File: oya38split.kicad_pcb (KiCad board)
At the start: 2 copper layers, 89 parts, among them M12 MX-NoLED, U1 ProMicro

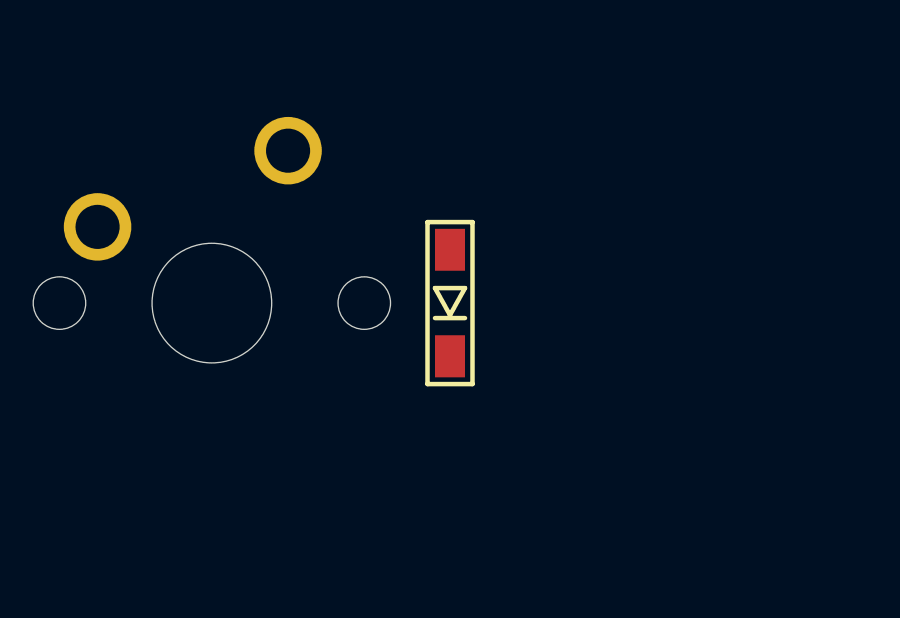
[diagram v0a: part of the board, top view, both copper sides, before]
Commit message: fixed diode alignment
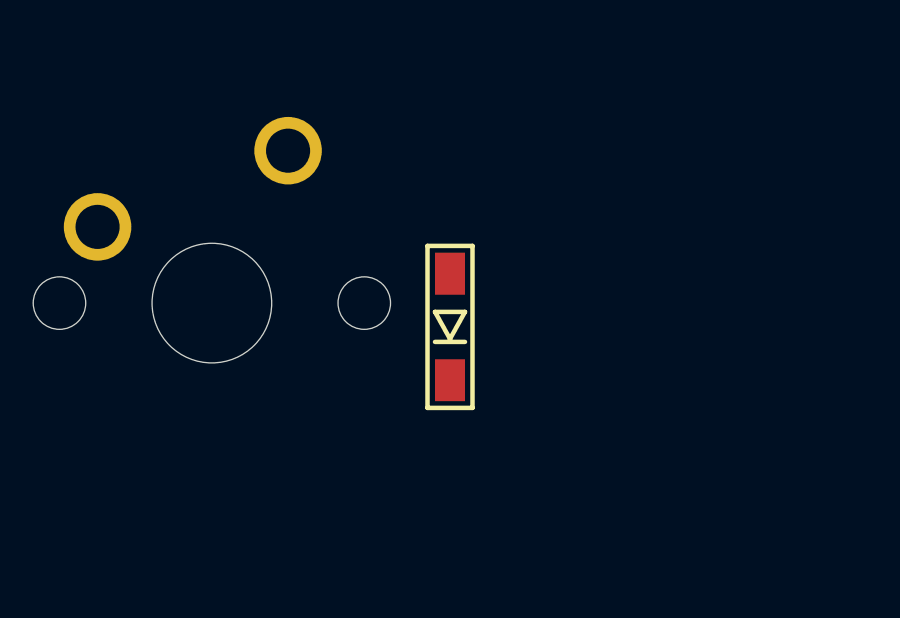
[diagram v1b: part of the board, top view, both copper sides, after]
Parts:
- moved D31 0.79 mm to (65.1, 115.1)
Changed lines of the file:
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@@
   )
   (module kbd:D3_SMD_v2 (layer F.Cu)
-    (at 65.0875 114.3 90)
+    (at 65.0875 115.09375 90)
     (descr "Resitance 3 pas")
     (tags R)

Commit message: fixing diodes and adding split
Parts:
- moved D36 69.9 mm to (249.2, 117.5)
- moved D43 69.9 mm to (281.0, 41.3)
- moved MX17 69.9 mm to (241.3, 78.6)
- moved MX18 69.9 mm to (260.4, 78.6)
- moved MX27 69.9 mm to (241.3, 97.6)
- moved MX28 69.9 mm to (260.4, 97.6)
- moved MX36 69.9 mm to (241.3, 116.7)
- moved MX37 69.9 mm to (260.4, 116.7)
- moved MX43 69.9 mm to (288.9, 40.5)
- moved MX7 69.9 mm to (241.3, 59.5)
- moved MX8 69.9 mm to (260.4, 59.5)
- moved D10 69.9 mm to (290.5, 60.3)
- moved D20 69.9 mm to (290.5, 79.4)
- moved D30 69.9 mm to (290.5, 98.4)
- moved D35 69.9 mm to (214.3, 117.5)
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
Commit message: organized layout
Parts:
- moved U1 187.8 mm to (-12.7, 46.8)
- moved MX39 45.6 mm to (167.8, 48.2), turned to 8 degrees
- moved MX40 45.4 mm to (186.6, 45.6), turned to 8 degrees
- moved D39 45.4 mm to (175.8, 47.9), turned to 98 degrees
- moved MX41 45.4 mm to (205.5, 42.9), turned to 8 degrees
- moved D41 45.3 mm to (213.5, 42.6), turned to 98 degrees
- moved D40 45.3 mm to (194.6, 45.2), turned to 98 degrees
- moved MX6 42.3 mm to (180.4, 65.7), turned to 8 degrees
- moved MX8 42.2 mm to (218.2, 60.4), turned to 8 degrees
- moved D8 42.1 mm to (226.1, 60.1), turned to 98 degrees
- moved MX7 42.1 mm to (199.3, 63.0), turned to 8 degrees
- moved D6 42.1 mm to (188.4, 65.4), turned to 98 degrees
- moved D7 42.0 mm to (207.3, 62.7), turned to 98 degrees
- moved MX42 39.8 mm to (230.1, 40.1), turned to 4 degrees
- moved D42 39.8 mm to (238.0, 40.4), turned to 94 degrees
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
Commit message: added pro micro location
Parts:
- moved U1 80.6 mm to (67.5, 38.1)
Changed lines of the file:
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@@
   )
   (module Keebio-Parts:ArduinoProMicro (layer F.Cu)
-    (at -12.7 46.83125)
+    (at 67.46875 38.1)
     (fp_text reference U1 (at 0 1.625) (layer F.SilkS) hide
       (effects (font (size 1.27 1.524) (thickness 0.2032)))

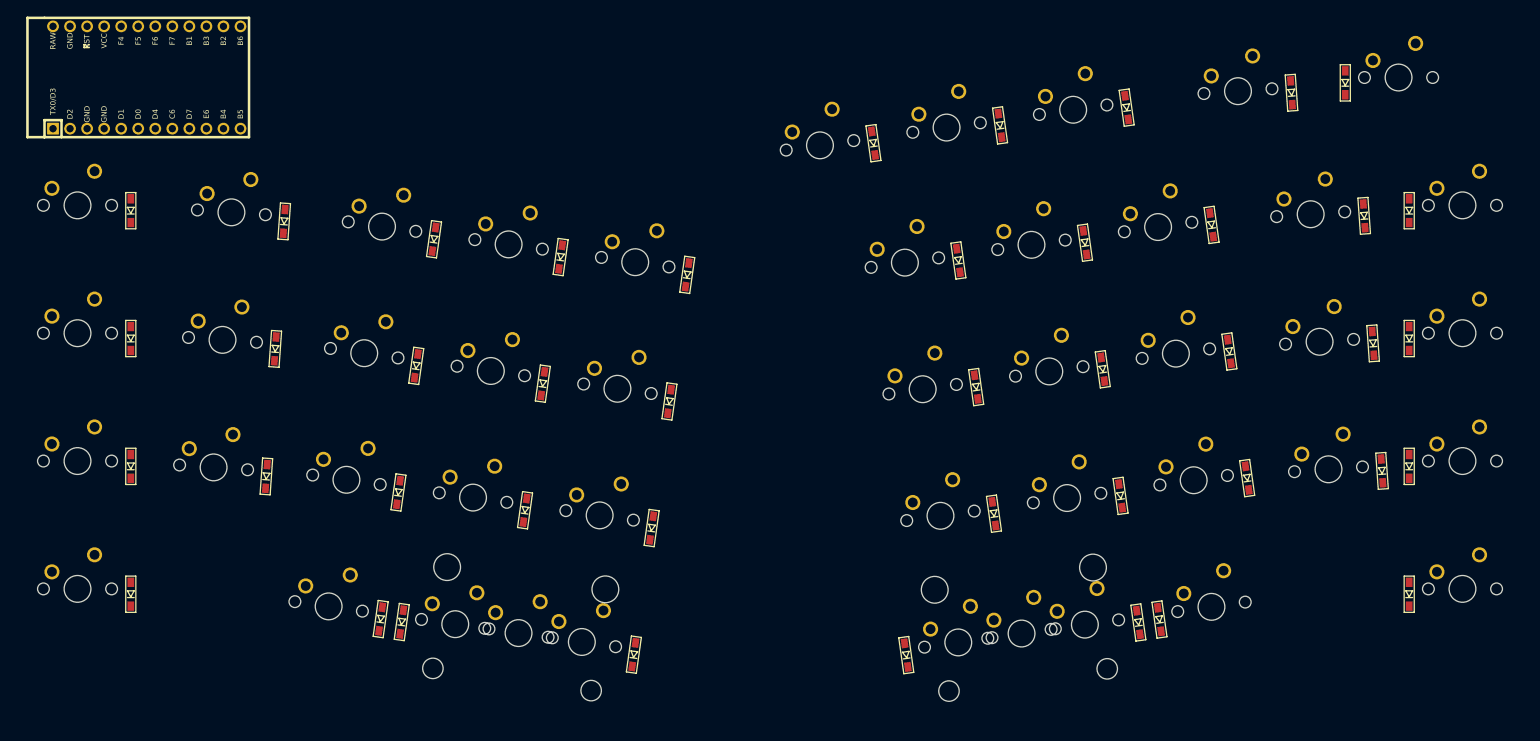
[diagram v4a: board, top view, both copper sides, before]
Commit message: added edge cuts and moved pro micro
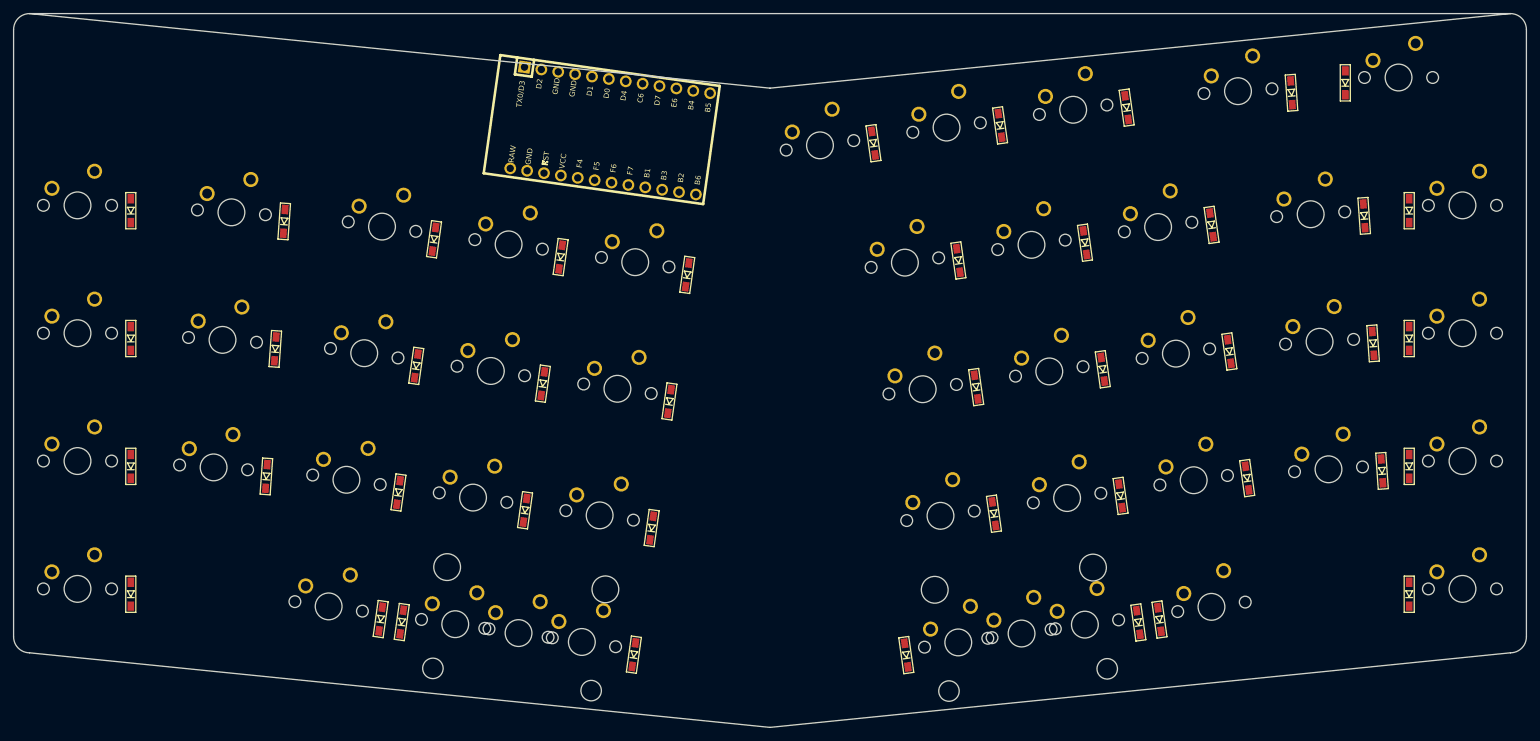
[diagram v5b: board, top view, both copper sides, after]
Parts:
- U1: moved to B.Cu
- moved U1 69.5 mm to (136.5, 46.0), turned to 352 degrees
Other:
- board outline added: 225.4 x 106.4 mm

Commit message: added traces
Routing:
- net Net-(D1-Pad1): track 0.00 -> 198.5 mm
- net Net-(D11-Pad1): track 0.00 -> 198.4 mm
- net Net-(D21-Pad1): track 0.00 -> 198.2 mm
- net Net-(D31-Pad1): track 0.00 -> 198.1 mm
- net Net-(MX16-Pad1): track 0.00 -> 92.6 mm
- net Net-(MX18-Pad1): track 0.00 -> 82.6 mm
- net Net-(MX17-Pad1): track 0.00 -> 82.6 mm
- net Net-(MX10-Pad1): track 0.00 -> 80.1 mm
- net Net-(D39-Pad1): track 0.00 -> 73.8 mm
- net Net-(MX15-Pad1): track 0.00 -> 69.9 mm
- net Net-(MX19-Pad1): track 0.00 -> 61.9 mm
- net Net-(MX14-Pad1): track 0.00 -> 60.8 mm
- net Net-(MX13-Pad1): track 0.00 -> 59.9 mm
- net Net-(MX1-Pad1): track 0.00 -> 57.2 mm
- net Net-(M12-Pad1): track 0.00 -> 39.1 mm
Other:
- outline, holes or cut-outs redrawn

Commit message: added traces
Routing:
- net Net-(D43-Pad2): track 0.00 -> 12.3 mm
- net Net-(D10-Pad2): track 0.00 -> 12.3 mm
- net Net-(D20-Pad2): track 0.00 -> 12.3 mm
- net Net-(D41-Pad2): track 0.00 -> 7.29 mm
- net Net-(D39-Pad2): track 0.00 -> 7.29 mm
- net Net-(D17-Pad2): track 0.00 -> 7.29 mm
- net Net-(D8-Pad2): track 0.00 -> 7.29 mm
- net Net-(D7-Pad2): track 0.00 -> 7.29 mm
- net Net-(D18-Pad2): track 0.00 -> 7.29 mm
- net Net-(D6-Pad2): track 0.00 -> 7.29 mm
- net Net-(D16-Pad2): track 0.00 -> 7.29 mm
- net Net-(D40-Pad2): track 0.00 -> 7.29 mm
- net Net-(D9-Pad2): track 0.00 -> 7.21 mm
- net Net-(D19-Pad2): track 0.00 -> 7.21 mm
- net Net-(D42-Pad2): track 0.00 -> 7.21 mm
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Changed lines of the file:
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@@
     (thickness 1.6)
     (drawings 9)
-    (tracks 187)
+    (tracks 240)
     (zones 0)
     (modules 89)
@@
   (gr_arc (start 270.66875 121.44375) (end 270.66875 123.825) (angle -90) (layer Edge.Cuts) (width 0.05))
   (gr_arc (start 270.66875 30.95625) (end 273.05 30.95625) (angle -90) (layer Edge.Cuts) (width 0.05))
+  (segment (start 63.78875 56.16875) (end 65.0875 56.16875) (width 0.25) (layer F.Cu) (net 1))
+  (segment (start 59.69 52.07) (end 63.78875 56.16875) (width 0.25) (layer F.Cu) (net 1))
   (segment (start 249.764339 59.71875) (end 249.0001 60.482989) (width 0.25) (layer F.Cu) (net 2))
   (segment (start 255.5875 59.71875) (end 249.764339 59.71875) (width 0.25) (layer F.Cu) (net 2))
@@
   (segment (start 66.475297 61.306547) (end 65.0875 59.91875) (width 0.25) (layer F.Cu) (net 2))
   (segment (start 87.826043 61.306547) (end 66.475297 61.306547) (width 0.25) (layer F.Cu) (net 2))
+  (segment (start 87.440517 57.765195) (end 88.073679 57.765195) (width 0.25) (layer F.Cu) (net 3))
+  (segment (start 82.975241 53.299919) (end 87.440517 57.765195) (width 0.25) (layer F.Cu) (net 3))
+  (segment (start 110.522531 60.411512) (end 110.522531 60.447024) (width 0.25) (layer F.Cu) (net 4))
+  (segment (start 105.747995 55.636976) (end 110.522531 60.411512) (width 0.25) (layer F.Cu) (net 4))
+  (segment (start 129.387138 63.062761) (end 129.387138 63.098271) (width 0.25) (layer F.Cu) (net 5))
+  (segment (start 124.612601 58.288224) (end 129.387138 63.062761) (width 0.25) (layer F.Cu) (net 5))
+  (segment (start 148.251745 65.714009) (end 148.251745 65.749519) (width 0.25) (layer F.Cu) (net 6))
+  (segment (start 143.477208 60.939472) (end 148.251745 65.714009) (width 0.25) (layer F.Cu) (net 6))
+  (segment (start 185.554657 63.60716) (end 188.16239 63.60716) (width 0.25) (layer F.Cu) (net 7))
+  (segment (start 182.246983 60.299486) (end 185.554657 63.60716) (width 0.25) (layer F.Cu) (net 7))
+  (segment (start 204.419262 60.955912) (end 207.026997 60.955912) (width 0.25) (layer F.Cu) (net 8))
+  (segment (start 201.111589 57.648239) (end 204.419262 60.955912) (width 0.25) (layer F.Cu) (net 8))
+  (segment (start 223.28387 58.304665) (end 225.891604 58.304665) (width 0.25) (layer F.Cu) (net 9))
+  (segment (start 219.976196 54.996991) (end 223.28387 58.304665) (width 0.25) (layer F.Cu) (net 9))
+  (segment (start 245.040209 53.229382) (end 248.752464 56.941637) (width 0.25) (layer F.Cu) (net 10))
+  (segment (start 243.082198 53.229382) (end 245.040209 53.229382) (width 0.25) (layer F.Cu) (net 10))
+  (segment (start 255.5875 55.96875) (end 255.5875 56.16875) (width 0.25) (layer F.Cu) (net 11))
+  (segment (start 259.48625 52.07) (end 255.5875 55.96875) (width 0.25) (layer F.Cu) (net 11))
+  (segment (start 266.065 52.07) (end 259.48625 52.07) (width 0.25) (layer F.Cu) (net 11))
+  (segment (start 63.78875 75.21875) (end 65.0875 75.21875) (width 0.25) (layer F.Cu) (net 12))
+  (segment (start 59.69 71.12) (end 63.78875 75.21875) (width 0.25) (layer F.Cu) (net 12))
   (segment (start 251.046795 78.76875) (end 250.328961 79.486584) (width 0.25) (layer F.Cu) (net 13))
   (segment (start 255.5875 78.76875) (end 251.046795 78.76875) (width 0.25) (layer F.Cu) (net 13))
@@
   (segment (start 66.428892 80.310142) (end 65.0875 78.96875) (width 0.25) (layer F.Cu) (net 13))
   (segment (start 86.497182 80.310142) (end 66.428892 80.310142) (width 0.25) (layer F.Cu) (net 13))
+  (segment (start 86.111657 76.76879) (end 86.744818 76.76879) (width 0.25) (layer F.Cu) (net 14))
+  (segment (start 81.646381 72.303514) (end 86.111657 76.76879) (width 0.25) (layer F.Cu) (net 14))
+  (segment (start 107.871284 79.27612) (end 107.871284 79.311631) (width 0.25) (layer F.Cu) (net 15))
+  (segment (start 103.096747 74.501583) (end 107.871284 79.27612) (width 0.25) (layer F.Cu) (net 15))
+  (segment (start 126.73589 81.927367) (end 126.73589 81.962878) (width 0.25) (layer F.Cu) (net 16))
+  (segment (start 121.961354 77.152831) (end 126.73589 81.927367) (width 0.25) (layer F.Cu) (net 16))
+  (segment (start 145.600497 84.578614) (end 145.600497 84.614126) (width 0.25) (layer F.Cu) (net 17))
+  (segment (start 140.825961 79.804078) (end 145.600497 84.578614) (width 0.25) (layer F.Cu) (net 17))
+  (segment (start 188.205904 82.471766) (end 190.813638 82.471766) (width 0.25) (layer F.Cu) (net 18))
+  (segment (start 184.898231 79.164093) (end 188.205904 82.471766) (width 0.25) (layer F.Cu) (net 18))
+  (segment (start 207.070511 79.820519) (end 209.678245 79.820519) (width 0.25) (layer F.Cu) (net 19))
+  (segment (start 203.762837 76.512845) (end 207.070511 79.820519) (width 0.25) (layer F.Cu) (net 19))
+  (segment (start 225.935119 77.169272) (end 228.542851 77.169272) (width 0.25) (layer F.Cu) (net 20))
+  (segment (start 222.627444 73.861597) (end 225.935119 77.169272) (width 0.25) (layer F.Cu) (net 20))
+  (segment (start 248.123314 75.945232) (end 250.081325 75.945232) (width 0.25) (layer F.Cu) (net 21))
+  (segment (start 244.411059 72.232977) (end 248.123314 75.945232) (width 0.25) (layer F.Cu) (net 21))
+  (segment (start 255.5875 75.01875) (end 255.5875 75.21875) (width 0.25) (layer F.Cu) (net 22))
+  (segment (start 259.48625 71.12) (end 255.5875 75.01875) (width 0.25) (layer F.Cu) (net 22))
+  (segment (start 266.065 71.12) (end 259.48625 71.12) (width 0.25) (layer F.Cu) (net 22))
   (segment (start 252.329251 97.81875) (end 251.657821 98.49018) (width 0.25) (layer F.Cu) (net 24))
   (segment (start 255.5875 97.81875) (end 252.329251 97.81875) (width 0.25) (layer F.Cu) (net 24))
@@
   (segment (start 68.575046 120.556296) (end 65.0875 117.06875) (width 0.25) (layer F.Cu) (net 35))
   (segment (start 102.074724 120.556296) (end 68.575046 120.556296) (width 0.25) (layer F.Cu) (net 35))
+  (segment (start 172.899332 46.131459) (end 175.507066 46.131459) (width 0.25) (layer F.Cu) (net 43))
+  (segment (start 169.591658 42.823785) (end 172.899332 46.131459) (width 0.25) (layer F.Cu) (net 43))
   (segment (start 239.644515 40.66875) (end 238.169441 42.143824) (width 0.25) (layer F.Cu) (net 44))
   (segment (start 246.0625 40.66875) (end 239.644515 40.66875) (width 0.25) (layer F.Cu) (net 44))
@@
   (segment (start 192.214489 49.646911) (end 176.00113 49.646911) (width 0.25) (layer F.Cu) (net 44))
   (segment (start 194.865736 46.995664) (end 192.214489 49.646911) (width 0.25) (layer F.Cu) (net 44))
+  (segment (start 191.763941 43.480212) (end 194.371672 43.480212) (width 0.25) (layer F.Cu) (net 45))
+  (segment (start 188.456266 40.172537) (end 191.763941 43.480212) (width 0.25) (layer F.Cu) (net 45))
+  (segment (start 210.628547 40.828964) (end 213.23628 40.828964) (width 0.25) (layer F.Cu) (net 46))
+  (segment (start 207.320872 37.521289) (end 210.628547 40.828964) (width 0.25) (layer F.Cu) (net 46))
+  (segment (start 234.20955 34.890217) (end 237.921805 38.602472) (width 0.25) (layer F.Cu) (net 47))
+  (segment (start 232.25154 34.890217) (end 234.20955 34.890217) (width 0.25) (layer F.Cu) (net 47))
+  (segment (start 246.0625 36.91875) (end 246.0625 37.11875) (width 0.25) (layer F.Cu) (net 48))
+  (segment (start 249.96125 33.02) (end 246.0625 36.91875) (width 0.25) (layer F.Cu) (net 48))
+  (segment (start 256.54 33.02) (end 249.96125 33.02) (width 0.25) (layer F.Cu) (net 48))
   (segment (start 76.259666 73.269374) (end 75.134667 74.394373) (width 0.25) (layer B.Cu) (net 49))
   (segment (start 76.439304 73.089736) (end 76.259666 73.269374) (width 0.25) (layer B.Cu) (net 49))

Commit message: layout
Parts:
- removed M12: MX-NoLED, MX_Only:MXOnly-1U-NoLED
- added MX12: MX-NoLED, MX_Only:MXOnly-1U-NoLED, F.Cu at (76.2, 76.2)
- MX10, MX16, MX17, MX18, MX19, MX20, MX26, MX27, MX28, MX29, MX30, MX35, MX36, MX37, MX38, MX39, MX40, MX41, MX42, MX43, MX45, MX6, MX7, MX8, MX9: moved to B.Cu
- U1: moved to F.Cu
- moved D38 459.3 mm to (-202.4, 80.4), turned to 0 degrees
- moved D30 451.6 mm to (-195.9, 85.7), turned to 0 degrees
- moved D42 441.8 mm to (-202.4, 75.1), turned to 0 degrees
- moved D29 441.1 mm to (-189.3, 80.4), turned to 0 degrees
- moved D19 439.6 mm to (-189.3, 85.7), turned to 0 degrees
- moved D20 438.4 mm to (-182.8, 83.1), turned to 0 degrees
- moved D43 436.7 mm to (-189.3, 72.5), turned to 0 degrees
- moved D37 422.3 mm to (-202.4, 83.1), turned to 0 degrees
- moved D10 419.1 mm to (-163.1, 76.5), turned to 0 degrees
- moved D28 414.8 mm to (-182.8, 75.1), turned to 0 degrees
- moved D36 412.9 mm to (-195.9, 80.4), turned to 0 degrees
- moved D18 411.6 mm to (-182.8, 85.7), turned to 0 degrees
- moved D41 410.6 mm to (-195.9, 75.1), turned to 0 degrees
- moved D9 405.8 mm to (-156.6, 76.5), turned to 0 degrees
- moved D40 398.4 mm to (-202.4, 77.8), turned to 0 degrees
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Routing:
- net Net-(D1-Pad1): track 198.5 -> 0.00 mm
- net Net-(D11-Pad1): track 198.4 -> 0.00 mm
- net Net-(D21-Pad1): track 198.2 -> 0.00 mm
- net Net-(D31-Pad1): track 198.1 -> 0.00 mm
- net Net-(MX16-Pad1): track 92.6 -> 0.00 mm
- net Net-(MX18-Pad1): track 82.6 -> 0.00 mm
- net Net-(MX17-Pad1): track 82.6 -> 0.00 mm
- net Net-(MX10-Pad1): track 80.1 -> 0.00 mm
- net Net-(D39-Pad1): track 73.8 -> 0.00 mm
- net Net-(MX15-Pad1): track 69.9 -> 0.00 mm
- net Net-(MX19-Pad1): track 61.9 -> 0.00 mm
- net Net-(MX14-Pad1): track 60.8 -> 0.00 mm
- net Net-(MX13-Pad1): track 59.9 -> 0.00 mm
- net Net-(MX1-Pad1): track 57.2 -> 0.00 mm
- net Net-(MX12-Pad1): track 39.1 -> 0.00 mm
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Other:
- board outline removed
